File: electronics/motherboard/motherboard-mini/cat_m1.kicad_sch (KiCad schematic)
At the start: 35 parts, among them J10 CONUFL001-SMD-T, J11 SIM8060-6-0-14-00-A, Q4 BC847, Q5 BC847, SW4 CAT_M1_RST, U10 TPS22967DSGR, U11 SARA-R410M-02B, U12 AOZ8904CIL, U13 TXB0104PW

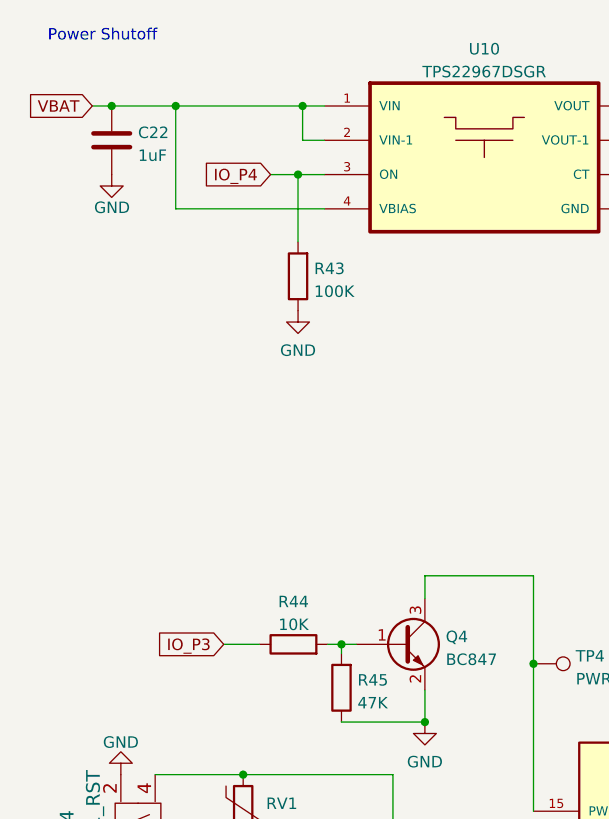
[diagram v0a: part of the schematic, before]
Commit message: added mounting circuit board and updated motherboard for next itteration
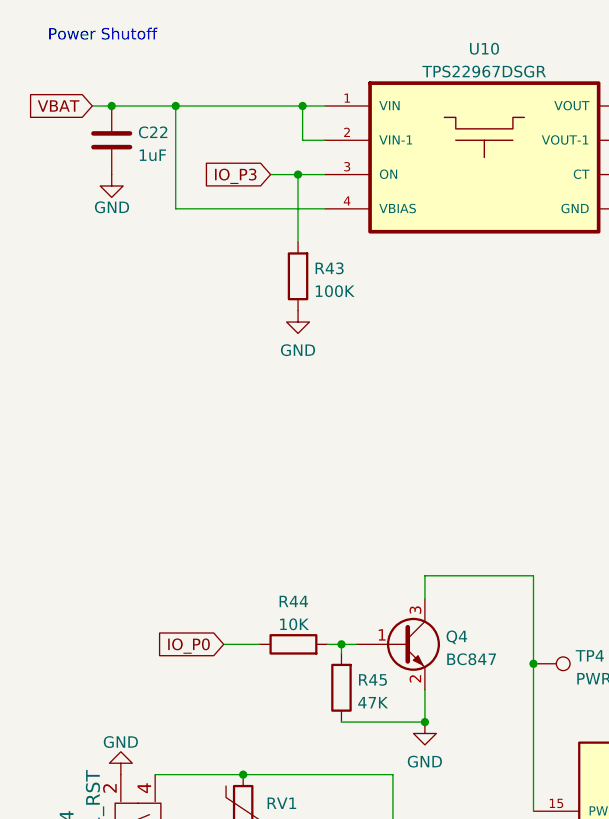
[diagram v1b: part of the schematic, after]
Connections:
- net IO_P4 is gone; now on net IO_P3: R43.2, U10.3 (ON)
- net IO_P3: no longer R44.1
- new net IO_P0: R44.1
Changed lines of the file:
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@@
     )
   )
-  (global_label "IO_P3" (shape input) (at 42.037 99.949 180) (fields_autoplaced)
+  (global_label "IO_P0" (shape input) (at 42.037 99.949 180) (fields_autoplaced)
     (effects (font (size 1.27 1.27)) (justify right))
-    (property "Intersheet References" "${INTERSHEET_REFS}" (id 0) (at 34.2415 100.0284 0)
+    (property "Intersheet References" "${INTERSHEET_REFS}" (id 0) (at 34.2415 99.8696 0)
       (effects (font (size 1.27 1.27)) (justify right) hide)
     )
@@
     )
   )
-  (global_label "IO_P4" (shape input) (at 47.244 47.752 180) (fields_autoplaced)
+  (global_label "IO_P3" (shape input) (at 47.244 47.752 180) (fields_autoplaced)
     (effects (font (size 1.27 1.27)) (justify right))
-    (property "Intersheet References" "${INTERSHEET_REFS}" (id 0) (at 39.4485 47.8314 0)
+    (property "Intersheet References" "${INTERSHEET_REFS}" (id 0) (at 39.4485 47.6726 0)
       (effects (font (size 1.27 1.27)) (justify right) hide)
     )

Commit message: added cat-m1 basic interface
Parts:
- removed R41, R42, R46: 0, Resistor_SMD:R_0805_2012Metric, symbol Device:R
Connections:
- net GND: now also U11.9 (DTR)
- net RX_1V8: now also U11.13 (RXD), U13.4 (A3); no longer U13.5 (A4)
- net TX_1V8: now also U11.12 (TXD), U13.5 (A4); no longer U13.4 (A3)
- net UART_RX1: now also U13.10 (B4); no longer U13.11 (B3)
- net UART_TX1: now also U13.11 (B3); no longer U13.10 (B4)
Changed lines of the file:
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@@
-    (stroke (width 0) (type default) (color 0 0 0 0))
-  )
-  (wire (pts (xy 71.247 165.735) (xy 74.168 165.735))
     (stroke (width 0) (type default) (color 0 0 0 0))
   )
@@
     (stroke (width 0) (type default) (color 0 0 0 0))
   )
-  (wire (pts (xy 61.214 165.735) (xy 63.627 165.735))
+  (wire (pts (xy 61.214 165.735) (xy 74.168 165.735))
     (stroke (width 0) (type default) (color 0 0 0 0))
   )
@@
     (stroke (width 0) (type default) (color 0 0 0 0))
   )
-  (wire (pts (xy 42.672 153.543) (xy 44.45 153.543))
-    (stroke (width 0) (type default) (color 0 0 0 0))
-  )
   (wire (pts (xy 64.389 92.329) (xy 76.454 92.329))
     (stroke (width 0) (type default) (color 0 0 0 0))
@@
   )
   (wire (pts (xy 29.591 40.132) (xy 36.703 40.132))
-    (stroke (width 0) (type default) (color 0 0 0 0))
-  )
-  (wire (pts (xy 42.672 146.431) (xy 44.577 146.431))
     (stroke (width 0) (type default) (color 0 0 0 0))
   )
@@
     (effects (font (size 1.27 1.27)) (justify left bottom))
   )
-  (global_label "UART_TX1" (shape input) (at 249.682 67.056 0) (fields_autoplaced)
+  (global_label "UART_TX1" (shape input) (at 249.682 61.976 0) (fields_autoplaced)
     (effects (font (size 1.27 1.27)) (justify left))
-    (property "Intersheet References" "${INTERSHEET_REFS}" (id 0) (at 261.1061 66.9766 0)
+    (property "Intersheet References" "${INTERSHEET_REFS}" (id 0) (at 261.1061 61.8966 0)
       (effects (font (size 1.27 1.27)) (justify left) hide)
     )
@@
     )
   )
-  (global_label "TX_1V8" (shape input) (at 42.672 146.431 180) (fields_autoplaced)
+  (global_label "TX_1V8" (shape input) (at 52.197 146.431 180) (fields_autoplaced)
     (effects (font (size 1.27 1.27)) (justify right))
-    (property "Intersheet References" "${INTERSHEET_REFS}" (id 0) (at 33.6065 146.3516 0)
+    (property "Intersheet References" "${INTERSHEET_REFS}" (id 0) (at 43.1315 146.3516 0)
       (effects (font (size 1.27 1.27)) (justify right) hide)
     )
   )
-  (global_label "RX_1V8" (shape input) (at 42.672 153.543 180) (fields_autoplaced)
+  (global_label "RX_1V8" (shape input) (at 52.07 153.543 180) (fields_autoplaced)
     (effects (font (size 1.27 1.27)) (justify right))
-    (property "Intersheet References" "${INTERSHEET_REFS}" (id 0) (at 33.3041 153.4636 0)
+    (property "Intersheet References" "${INTERSHEET_REFS}" (id 0) (at 42.7021 153.4636 0)
       (effects (font (size 1.27 1.27)) (justify right) hide)
     )
@@
     )
   )
-  (global_label "TX_1V8" (shape input) (at 229.362 61.976 180) (fields_autoplaced)
+  (global_label "TX_1V8" (shape input) (at 229.362 67.056 180) (fields_autoplaced)
     (effects (font (size 1.27 1.27)) (justify right))
-    (property "Intersheet References" "${INTERSHEET_REFS}" (id 0) (at 220.2965 62.0554 0)
+    (property "Intersheet References" "${INTERSHEET_REFS}" (id 0) (at 220.2965 67.1354 0)
       (effects (font (size 1.27 1.27)) (justify right) hide)
     )
   )
-  (global_label "UART_RX1" (shape input) (at 249.682 61.976 0) (fields_autoplaced)
+  (global_label "UART_RX1" (shape input) (at 249.682 67.056 0) (fields_autoplaced)
     (effects (font (size 1.27 1.27)) (justify left))
-    (property "Intersheet References" "${INTERSHEET_REFS}" (id 0) (at 261.4084 61.8966 0)
+    (property "Intersheet References" "${INTERSHEET_REFS}" (id 0) (at 261.4084 66.9766 0)
       (effects (font (size 1.27 1.27)) (justify left) hide)
     )
@@
     )
   )
-  (global_label "RX_1V8" (shape input) (at 229.362 67.056 180) (fields_autoplaced)
+  (global_label "RX_1V8" (shape input) (at 229.362 61.976 180) (fields_autoplaced)
     (effects (font (size 1.27 1.27)) (justify right))
-    (property "Intersheet References" "${INTERSHEET_REFS}" (id 0) (at 219.9941 67.1354 0)
+    (property "Intersheet References" "${INTERSHEET_REFS}" (id 0) (at 219.9941 62.0554 0)
       (effects (font (size 1.27 1.27)) (justify right) hide)
     )
@@
     )
     (pin "1")
-  )
-  (symbol (lib_id "Device:R") (at 67.437 165.735 90) (unit 1)
-    (in_bom yes) (on_board yes) (fields_autoplaced)
-    (property "Reference" "R46" (id 0) (at 67.437 161.0192 90))
-    (property "Value" "0" (id 1) (at 67.437 163.5561 90))
-    (property "Footprint" "Resistor_SMD:R_0805_2012Metric" (id 2) (at 67.437 167.513 90)
-      (effects (font (size 1.27 1.27)) hide)
-    )
-    (property "Datasheet" "~" (id 3) (at 67.437 165.735 0)
-      (effects (font (size 1.27 1.27)) hide)
-    )
-    (pin "1")
-    (pin "2")
   )
   (symbol (lib_id "power:GND") (at 50.292 62.865 0) (unit 1)
@@
     )
     (pin "1")
-  )
-  (symbol (lib_id "Device:R") (at 48.26 153.543 90) (unit 1)
-    (in_bom yes) (on_board yes) (fields_autoplaced)
-    (property "Reference" "R41" (id 0) (at 48.26 148.8272 90))
-    (property "Value" "0" (id 1) (at 48.26 151.3641 90))
-    (property "Footprint" "Resistor_SMD:R_0805_2012Metric" (id 2) (at 48.26 155.321 90)
-      (effects (font (size 1.27 1.27)) hide)
-    )
-    (property "Datasheet" "~" (id 3) (at 48.26 153.543 0)
-      (effects (font (size 1.27 1.27)) hide)
-    )
-    (pin "1")
-    (pin "2")
   )
   (symbol (lib_id "power:GND") (at 95.123 50.292 0) (unit 1)
@@
       (effects (font (size 1.27 1.27)) hide)
     )
-    (pin "1")
-    (pin "2")
-  )
-  (symbol (lib_id "Device:R") (at 48.387 146.431 90) (unit 1)
-    (in_bom yes) (on_board yes) (fields_autoplaced)
-    (property "Reference" "R42" (id 0) (at 48.387 141.7152 90))
-    (property "Value" "0" (id 1) (at 48.387 144.2521 90))
-    (property "Footprint" "Resistor_SMD:R_0805_2012Metric" (id 2) (at 48.387 148.209 90)
-      (effects (font (size 1.27 1.27)) hide)
-    )
-    (property "Datasheet" "~" (id 3) (at 48.387 146.431 0)
-      (effects (font (size 1.27 1.27)) hide)
-    )

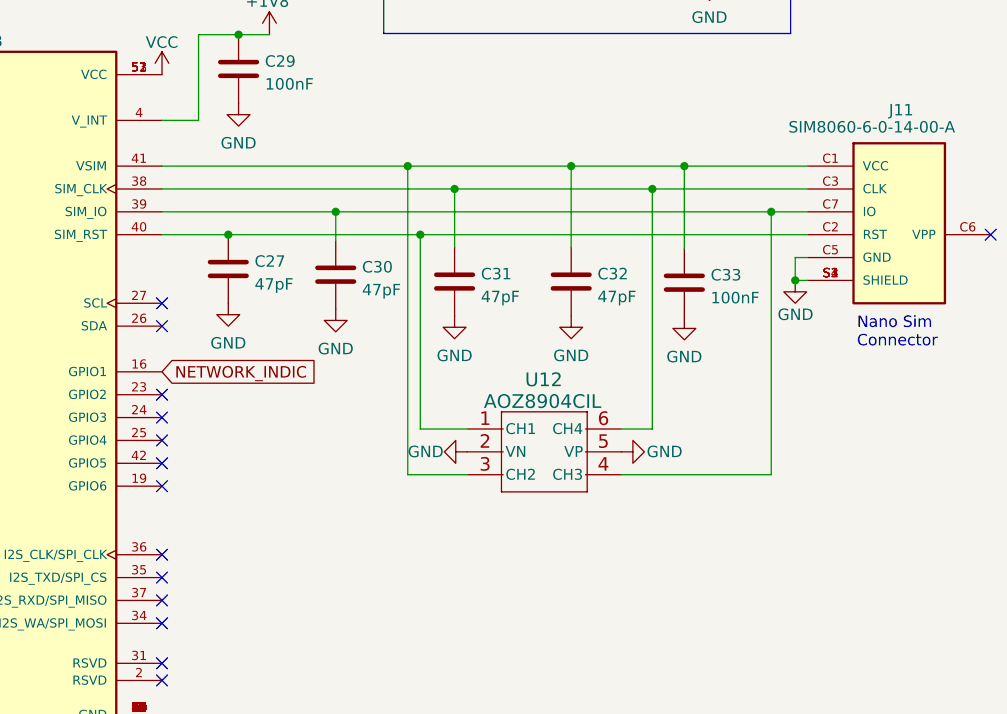
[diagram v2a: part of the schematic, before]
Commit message: added ble uart bidirectional tests
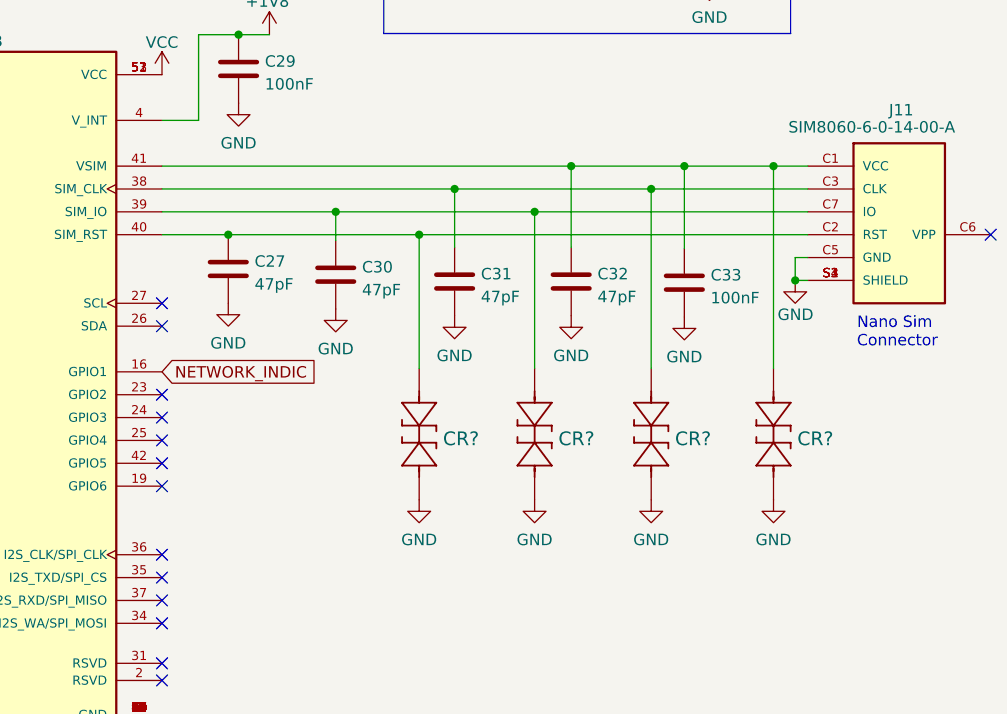
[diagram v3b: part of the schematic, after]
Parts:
- removed U12: AOZ8904CIL, AOZ8904CIL:AOZ8904CIL, symbol AOZ8904CIL:AOZ8904CIL
- added CR? (x4): PESD0402-140, PESD0402, symbol PESD0402-140:PESD0402-140
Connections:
- net GND: now also CR?.2, CR?.2, CR?.2, CR?.2
- net at C32.1, C33.1, J11.C1 (VCC)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: now also CR?.1
- net at C27.1, J11.C2 (RST), U11.40 (SIM_RST): now also CR?.1
- net at C30.1, J11.C7 (IO), U11.39 (SIM_IO): now also CR?.1
- net at C31.1, J11.C3 (CLK), U11.38 (SIM_CLK): now also CR?.1

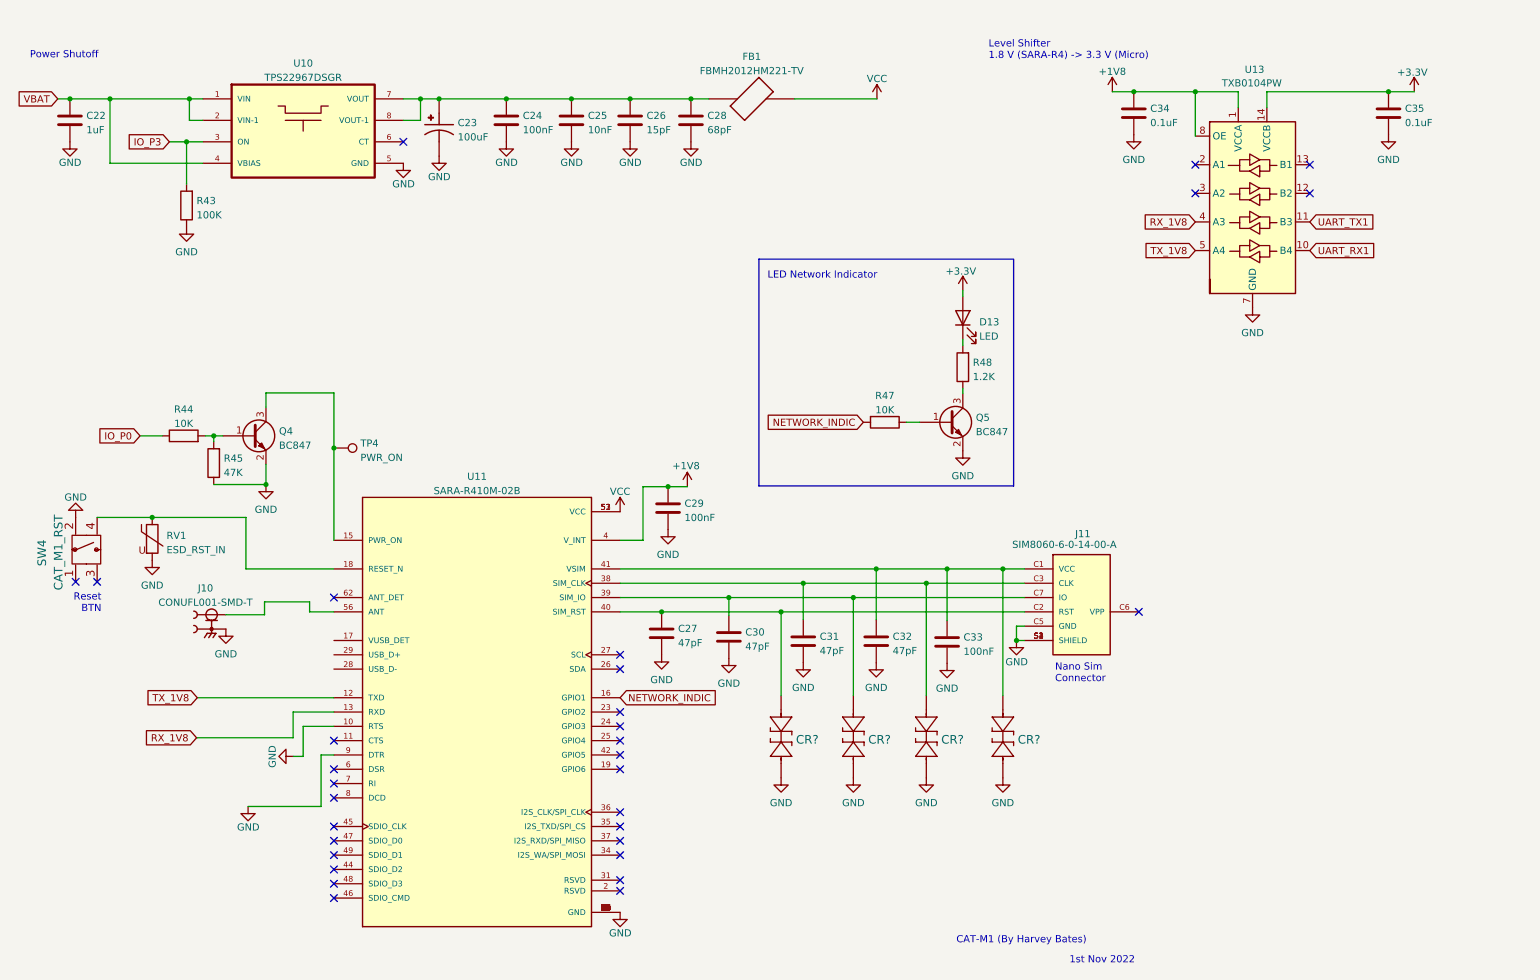
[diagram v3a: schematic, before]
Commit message: new board version sent for production, termed 'wombat' and breakout board
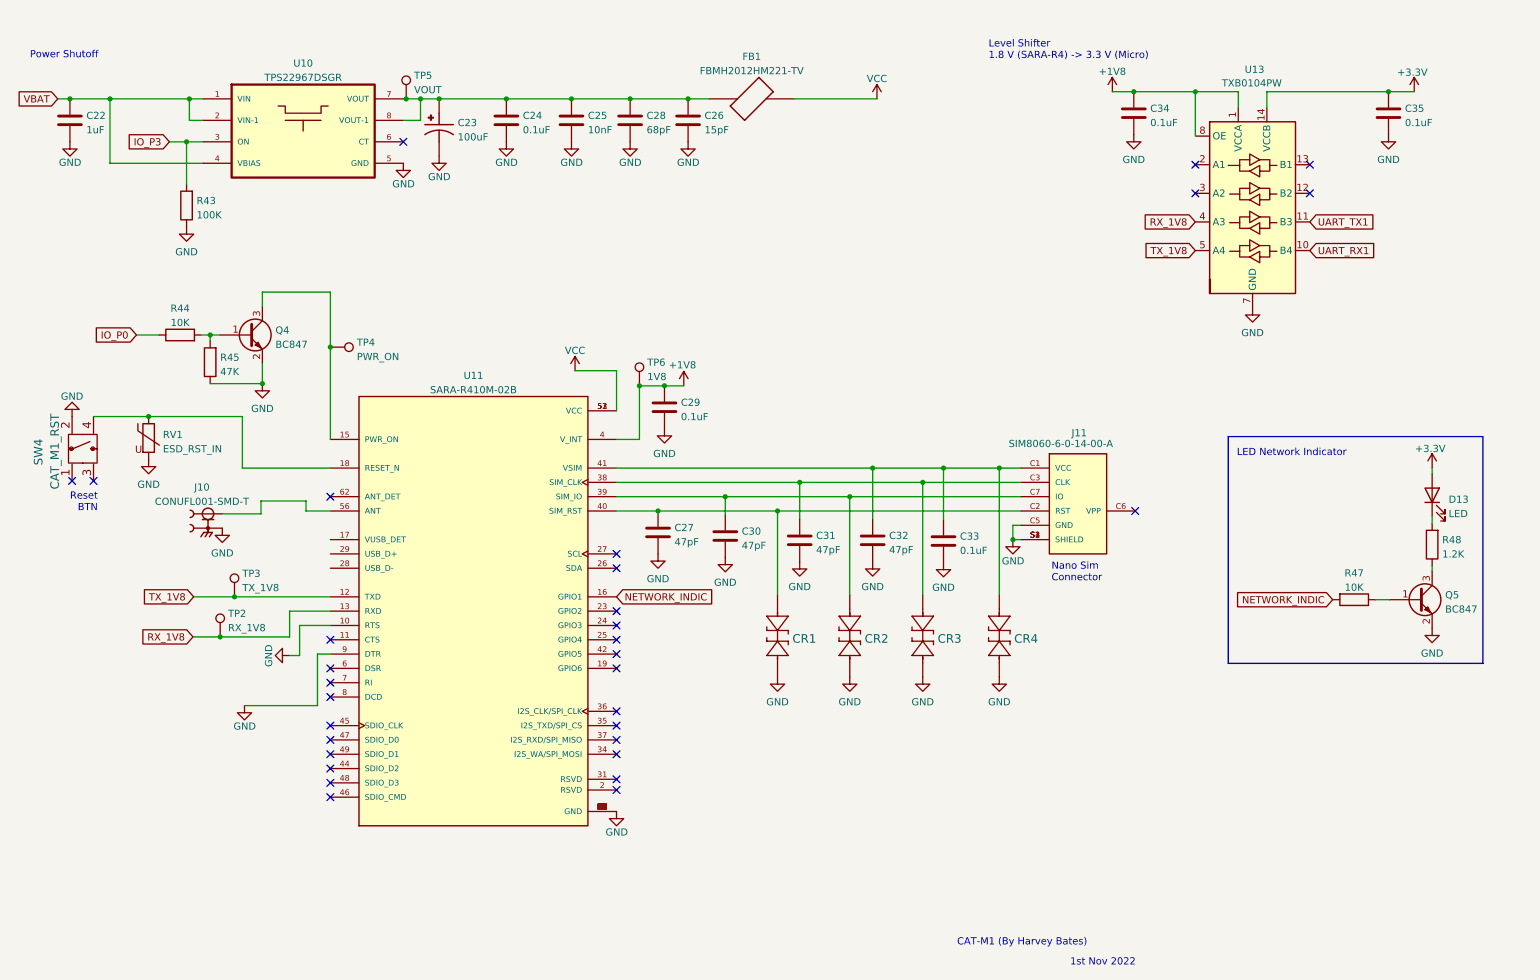
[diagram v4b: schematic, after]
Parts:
- added TP2: RX_1V8, TestPoint:TestPoint_Pad_D1.0mm, symbol Connector:TestPoint
- added TP3: TX_1V8, TestPoint:TestPoint_Pad_D1.0mm, symbol Connector:TestPoint
- added TP5: VOUT, TestPoint:TestPoint_Pad_D1.0mm, symbol Connector:TestPoint
- added TP6: 1V8, TestPoint:TestPoint_Pad_D1.0mm, symbol Connector:TestPoint
- C24, C29, C33: value 100nF -> 0.1uF
- CR1, CR2, CR3, CR4: renamed from CR?; footprint PESD0402 -> PESD0402-140:PESD0402-140
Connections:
- net +1V8: now also TP6.1
- net RX_1V8: now also TP2.1
- net TX_1V8: now also TP3.1
- net at C23.1, C24.1, C25.1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: now also TP5.1
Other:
- moved on the sheet: C26, C27, C28, C29, C30, C31, C32, C33, CR1, CR2, CR3, CR4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

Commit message: added component information for all items in motherboard
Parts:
- C22: Part (none) -> C0805C105K3RAC7800
- C23: Part (none) -> T520B107M006ATE015
- C24, C29, C33, C34, C35: Part (none) -> AC0805KRX7R7BB104
- C25: Part (none) -> C0805C103J5GEC7210
- C26: Part (none) -> C0805C150J3GAC7800
- C27, C30, C31, C32: Part (none) -> C0805C470K5RAC7800
- C28: Part (none) -> C0805C680K5RACAUTO
- CR1, CR2, CR3, CR4: Part (none) -> PESD0402-140
- D13: value LED -> LED(Orange); Part (none) -> LO R976-PS-1
- FB1: Part (none) -> FBMH2012HM221-TV
- J10: Part (none) -> CONUFL001-SMD-T
- J11: Part (none) -> SIM8060-6-0-14-00-A
- R43: Part (none) -> CRCW0805100KJNTA
- R44: Part (none) -> https://www.digikey.com.au/en/products/detail/yageo/RC0805F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
- R47: Part (none) -> RC0805FR-0710KP
- R48: value 1.2K -> 1K
- RV1: Component VC080518A400DP -> (none); Part (none) -> VC080518A400DP
- SW4: Part (none) -> 1977223-6
- U10: Part (none) -> TPS22967DSGR
- U11: MANUFACTURER U-Blox -> (none); MAXIMUM_PACKAGE_HEIGHT 2.78 mm -> (none); PARTREV R20 -> (none); Part (none) -> SARA-R410M-02B; STANDARD Manufacturer Recommendations -> (none)
- U13: Part (none) -> TXB0104PW
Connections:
- net GND: now also C22.1; no longer C22.2
- net VBAT: now also C22.2; no longer C22.1
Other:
- note added: "Alternative part neeeded (ESDA18-1K possible)"

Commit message: new version sent for manufacture, updated component positioning, removed level shifter on SDI-12 line, re routed the solar charge circuit
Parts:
- removed C34: 0.1uF, Capacitor_SMD:C_0805_2012Metric, symbol Device:C
- renumbered C28 to C26, C29 to C28, C26 to C29, C35 to C34, D13 to D11, J10 to J11, J11 to J12, R44 to R36, R43 to R37, R45 to R38, R47 to R39, R48 to R40, SW4 to SW3, U10 to U11, U11 to U12
